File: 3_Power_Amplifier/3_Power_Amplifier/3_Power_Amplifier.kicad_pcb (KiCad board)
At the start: 2 copper layers, 100 x 100 mm, 15 parts, among them P1 IN_FUENTE_CONM, P2 OUT_CON_CAP, P3 OUT_SIN_CAP, P4 CONN_01X02, Q1 IRF740N, Q2 IRF740N, Q3 IRF740N, Q4 IRF740N, T1 TRANSFO-SO12

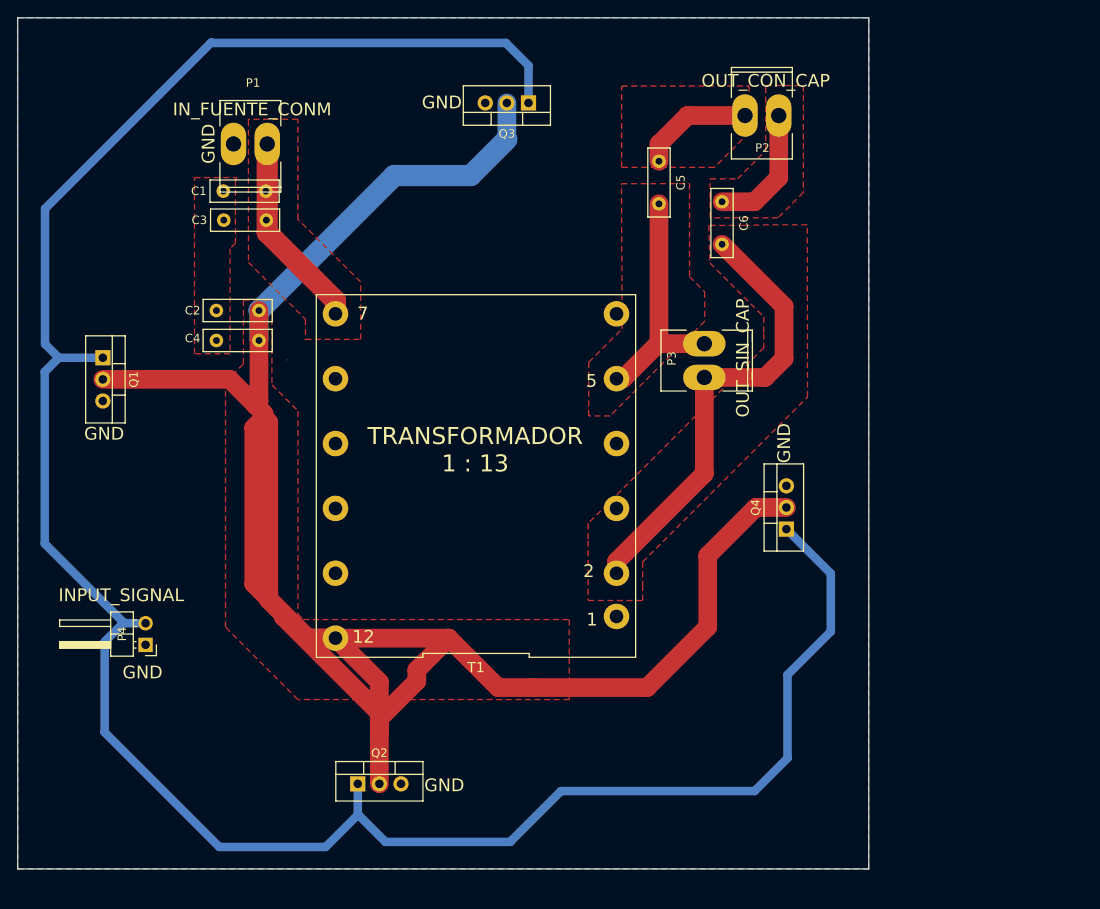
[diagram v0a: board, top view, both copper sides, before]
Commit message: AMPLIFICADOR DE POTENCIA_2 PCBS
el transformador con array capacitivo y mosfet con disipadores
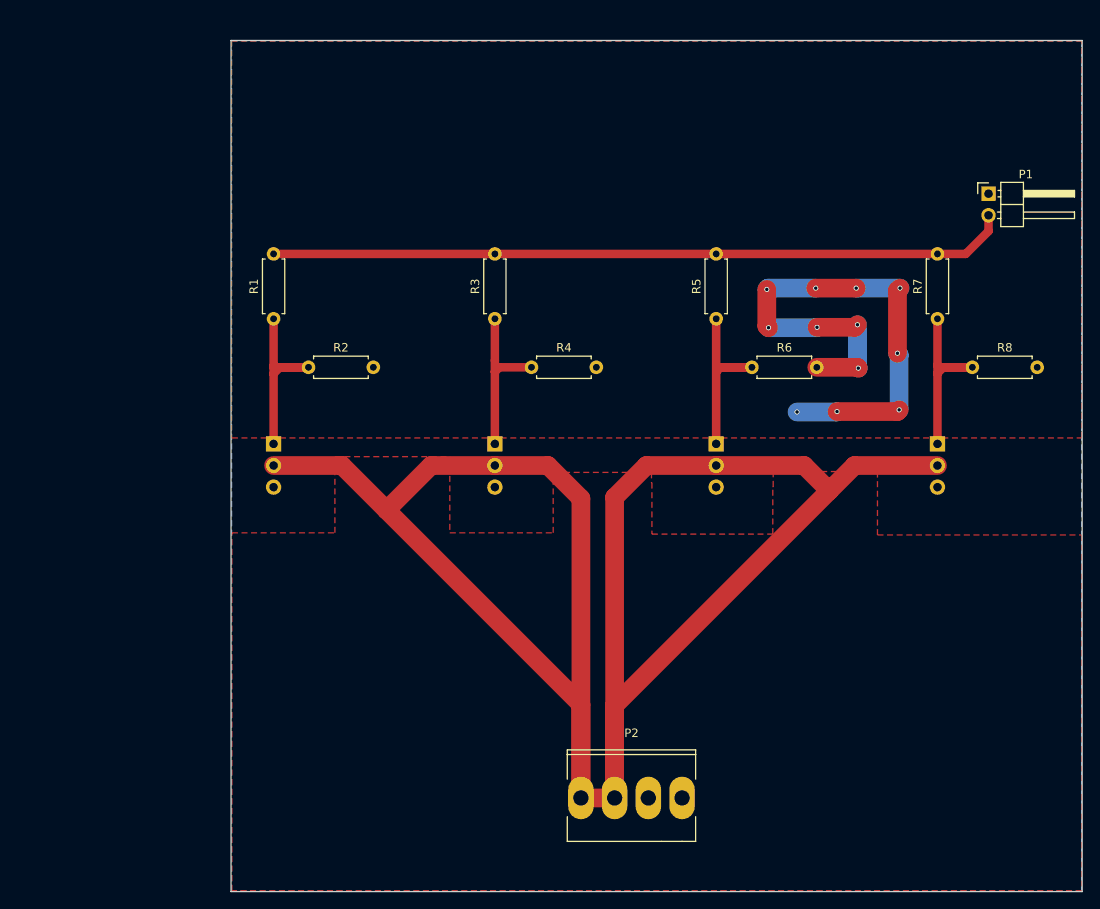
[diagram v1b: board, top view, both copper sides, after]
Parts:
- removed C1, C2, C3, C4, C5, C6: 32nF, Capacitors_THT:C_Disc_D8.0mm_W2.5mm_P5.00mm
- removed P3: OUT_SIN_CAP, Sockets_MOLEX_KK-System:Socket_MOLEX-KK-RM3-96mm_Lock_2pin_straight
- removed P4: CONN_01X02, Pin_Headers:Pin_Header_Angled_1x02_Pitch2.54mm
- removed T1: TRANSFO-SO12, libreria_Power_Amplifier_huellas:foot_print_trafo
- added R1: 100, Resistors_THT:R_Axial_DIN0207_L6.3mm_D2.5mm_P7.62mm_Horizontal, F.Cu at (83.5, 78.2)
- added R2: 10K, Resistors_THT:R_Axial_DIN0207_L6.3mm_D2.5mm_P7.62mm_Horizontal, F.Cu at (87.6, 83.9)
- added R3: 100, Resistors_THT:R_Axial_DIN0207_L6.3mm_D2.5mm_P7.62mm_Horizontal, F.Cu at (109.5, 78.2)
- added R4: 10K, Resistors_THT:R_Axial_DIN0207_L6.3mm_D2.5mm_P7.62mm_Horizontal, F.Cu at (113.8, 83.9)
- added R5: 100, Resistors_THT:R_Axial_DIN0207_L6.3mm_D2.5mm_P7.62mm_Horizontal, F.Cu at (135.5, 78.2)
- added R6: 10K, Resistors_THT:R_Axial_DIN0207_L6.3mm_D2.5mm_P7.62mm_Horizontal, F.Cu at (139.7, 83.9)
- added R7: 100, Resistors_THT:R_Axial_DIN0207_L6.3mm_D2.5mm_P7.62mm_Horizontal, F.Cu at (161.5, 78.2)
- added R8: 10K, Resistors_THT:R_Axial_DIN0207_L6.3mm_D2.5mm_P7.62mm_Horizontal, F.Cu at (165.6, 83.9)
- P1: value IN_FUENTE_CONM -> INPUT_SIGNAL; footprint Sockets_MOLEX_KK-System:Socket_MOLEX-KK-RM3-96mm_Lock_2pin_straight -> Pin_Headers:Pin_Header_Angled_1x02_Pitch2.54mm
- P2: value OUT_CON_CAP -> OUT_SWITCHEO; footprint Sockets_MOLEX_KK-System:Socket_MOLEX-KK-RM3-96mm_Lock_2pin_straight -> Sockets_MOLEX_KK-System:Socket_MOLEX-KK-RM3-96mm_Lock_4pin_straight
- Q1, Q2, Q3, Q4: footprint TO_SOT_Packages_THT:TO-220_Vertical -> libreria_Power_Amplifier_huellas:TO-220_Vertical
- moved P1 86.9 mm to (167.5, 63.5), turned to 0 degrees
- moved P2 81.6 mm to (125.5, 134.5)
- moved Q3 45.7 mm to (135.5, 92.9), turned to 270 degrees
- moved Q2 43.1 mm to (109.5, 92.9), turned to 270 degrees
- moved Q1 22.5 mm to (83.5, 92.9)
- moved Q4 20.4 mm to (161.5, 92.9), turned to 270 degrees
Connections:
- P1 pad 1: /ARRAY_CAP -> /GND
- P1 pad 2: /GND -> /DDS
- P2 pad 1: /OUT_SISTEM_ONE -> /SWITCHEO
- P2 pad 2: /OUT_SISTEM_TWO -> /SWITCHEO
- Q1 pad 1: /INPUT_SIGNAL -> Net-(Q1-Pad1)
- Q1 pad 2: /SIGNAL_PWM -> /SWITCHEO
- Q2 pad 1: /INPUT_SIGNAL -> Net-(Q2-Pad1)
- Q2 pad 2: /SIGNAL_PWM -> /SWITCHEO
- Q3 pad 1: /INPUT_SIGNAL -> Net-(Q3-Pad1)
- Q3 pad 2: /SIGNAL_PWM -> /SWITCHEO
- Q4 pad 1: /INPUT_SIGNAL -> Net-(Q4-Pad1)
- Q4 pad 2: /SIGNAL_PWM -> /SWITCHEO
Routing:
- net /INPUT_SIGNAL: track 273.5 -> 0.00 mm
- net /SIGNAL_PWM: track 260.3 -> 0.00 mm
- net /SWITCHEO: track 0.00 -> 248.3 mm
- net /DDS: track 0.00 -> 87.0 mm
- net /GND: track 0.00 -> 67.6 mm, vias 0 -> 12
- net /OUT_POT_TWO: track 54.0 -> 0.00 mm
- net /ARRAY_CAP: track 37.7 -> 0.00 mm
- net /OUT_POT_ONE: track 28.5 -> 0.00 mm
- net Net-(Q1-Pad1): track 0.00 -> 23.5 mm
- net Net-(Q3-Pad1): track 0.00 -> 23.3 mm
- net Net-(Q4-Pad1): track 0.00 -> 23.3 mm
- net Net-(Q2-Pad1): track 0.00 -> 19.2 mm
- net /OUT_SISTEM_TWO: track 15.1 -> 0.00 mm
- net /OUT_SISTEM_ONE: track 13.5 -> 0.00 mm
- added copper zone on F.Cu, net /GND
- added copper zone on F.Cu, net /SWITCHEO
- removed copper zone on F.Cu, net /ARRAY_CAP
- removed copper zone on F.Cu, net /OUT_POT_ONE
- removed copper zone on F.Cu, net /OUT_POT_TWO
- removed copper zone on F.Cu, net /OUT_SISTEM_ONE
- removed copper zone on F.Cu, net /OUT_SISTEM_TWO
- removed copper zone on F.Cu, net /SIGNAL_PWM
- removed copper zone on F.Cu, net Net-(C1-Pad2)
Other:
- board text removed: "1"
- board text removed: "12"
- board text removed: "2"
- board text removed: "5"
- board text removed: "7"
- board text removed: "GND"
- board text removed: "INPUT_SIGNAL"
- board text removed: "IN_FUENTE_CONM"
- board text removed: "OUT_CON_CAP"
- board text removed: "OUT_SIN_CAP"
- board text removed: "TRANSFORMADOR 1 : 13"

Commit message: AMPLIFICADOR DE POTENCIA_2 PCB_UNO
CON ISLETAS Y DISIPADORES VERTICALES
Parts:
- added P3: ISLETA, Mounting_Holes:MountingHole_3.2mm_M3_Pad_Via, F.Cu at (84.5, 139.5)
- added P4: ISLETA, Mounting_Holes:MountingHole_3.2mm_M3_Pad_Via, F.Cu at (172.5, 139.5)
- added P5: ISLETA, Mounting_Holes:MountingHole_3.2mm_M3_Pad_Via, F.Cu at (172.5, 51.5)
- added P6: ISLETA, Mounting_Holes:MountingHole_3.2mm_M3_Pad_Via, F.Cu at (84.5, 51.5)
- added P7: OUT_SWITCHEO, libreria_Power_Amplifier_huellas:Socket_MOLEX-2-pin-invertido, F.Cu at (124.6, 51.4)
- added P8: TIERRAA, Pin_Headers:Pin_Header_Straight_1x02_Pitch2.54mm, F.Cu at (83.0, 101.0)
- P1: footprint Pin_Headers:Pin_Header_Angled_1x02_Pitch2.54mm -> libreria_Power_Amplifier_huellas:Pin_Header_Pitch2.54mm_NEW
- P2: value OUT_SWITCHEO -> TIERRA; footprint Sockets_MOLEX_KK-System:Socket_MOLEX-KK-RM3-96mm_Lock_4pin_straight -> libreria_Power_Amplifier_huellas:Socket_MOLEX-2-pin-invertido
- Q1, Q2, Q3, Q4: value IRF740N -> IRF740NPBF; footprint libreria_Power_Amplifier_huellas:TO-220_Vertical -> libreria_Power_Amplifier_huellas:TO-220_Ver_Disipador
- R1, R2, R3, R4, R5, R6, R7, R8: footprint Resistors_THT:R_Axial_DIN0207_L6.3mm_D2.5mm_P7.62mm_Horizontal -> libreria_Power_Amplifier_huellas:R_Axia_P7.62mm_Horizontal_INV
- moved P1 84.7 mm to (128.4, 138.6), turned to 270 degrees
- moved P2 83.4 mm to (132.2, 51.4)
- moved R1 33.3 mm to (103.2, 105.1), turned to 270 degrees
- moved R3 30.5 mm to (123.6, 105.2), turned to 270 degrees
- moved R2 29.4 mm to (108.0, 105.1), turned to 270 degrees
- moved R5 28.4 mm to (144.9, 105.0), turned to 270 degrees
- moved R7 27.6 mm to (165.5, 105.5), turned to 270 degrees
- moved R4 25.9 mm to (128.5, 105.2), turned to 270 degrees
- moved R6 23.1 mm to (149.1, 105.0), turned to 270 degrees
- moved R8 22.0 mm to (170.0, 105.5), turned to 270 degrees
- moved Q1 18.7 mm to (102.0, 95.5)
- moved Q2 12.8 mm to (122.0, 95.5)
- moved Q3 7.94 mm to (143.0, 95.5)
- moved Q4 3.00 mm to (163.0, 95.5)
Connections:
- P1 pad 1: /GND -> /DDS
- P1 pad 2: /DDS -> /GND
- P2 pad 1: /SWITCHEO -> /GND
- P2 pad 2: /SWITCHEO -> /GND
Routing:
- net /SWITCHEO: track 248.3 -> 0.00 mm
- net /DDS: track 87.0 -> 0.00 mm
- net /GND: track 67.6 -> 28.2 mm, vias 12 -> 6
- net Net-(Q1-Pad1): track 23.5 -> 12.4 mm
- net Net-(Q3-Pad1): track 23.3 -> 12.3 mm
- net Net-(Q4-Pad1): track 23.3 -> 13.6 mm
- net Net-(Q2-Pad1): track 19.2 -> 13.2 mm
- added copper zone on F.Cu, net /DDS
- added copper zone on F.Cu, net Net-(Q1-Pad1)
- added copper zone on F.Cu, net Net-(Q2-Pad1)
- added copper zone on F.Cu, net Net-(Q3-Pad1)
- added copper zone on F.Cu, net Net-(Q4-Pad1)
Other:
- board text added: "3_POWER AMPLIFIER PART_1"
- board text added: "DDS"
- board text added: "GND"
- board text added: "SWITCHEO"

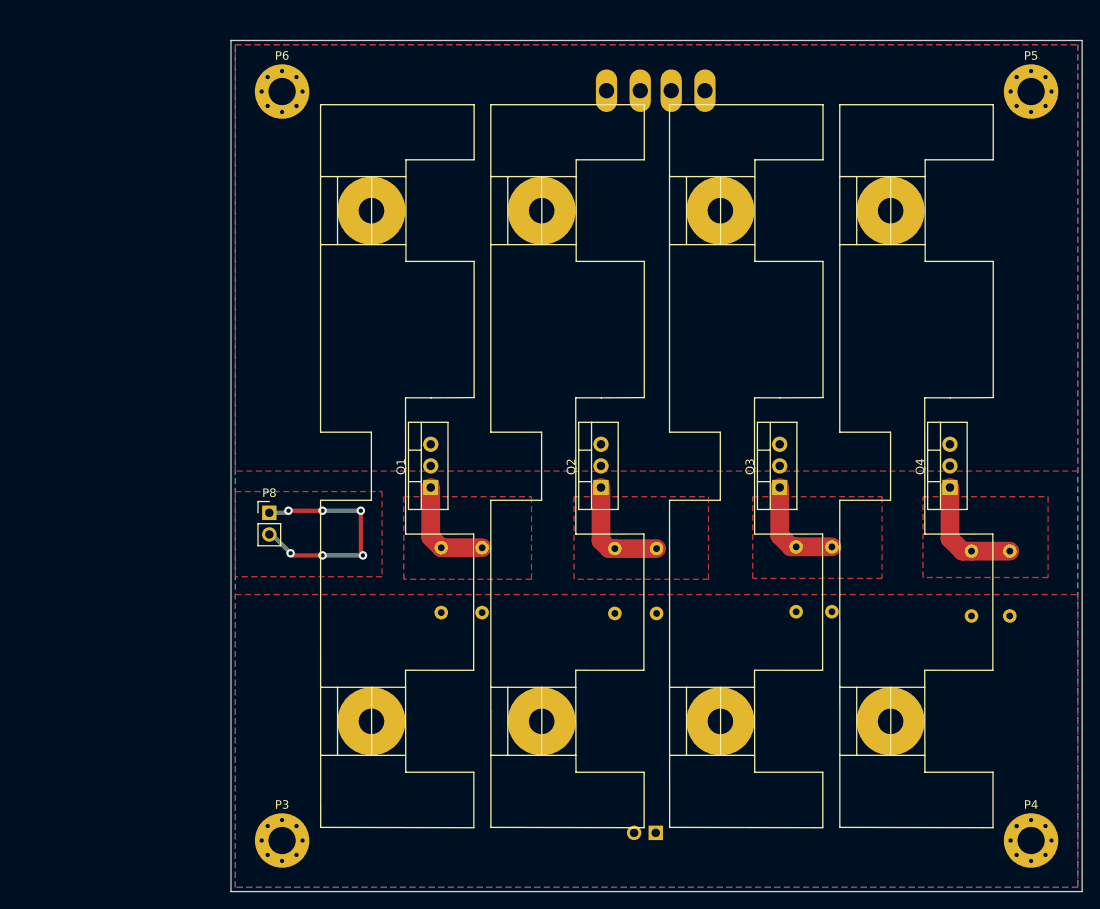
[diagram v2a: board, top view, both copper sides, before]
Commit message: AMPLIFICADOR DE POTENCIA_2 PCB_V3
MODIFICACION DE HUELLAS DEL COOLER Y PLANOS A SOLIDOS
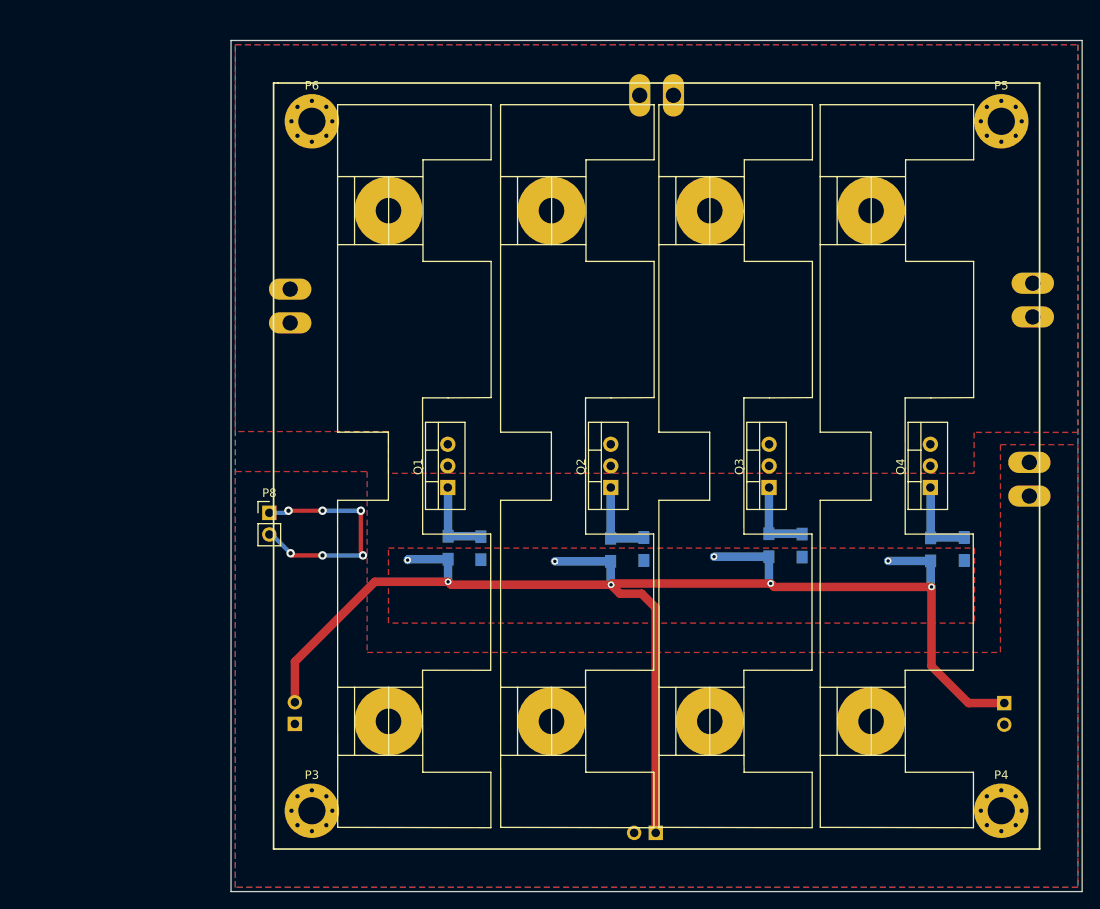
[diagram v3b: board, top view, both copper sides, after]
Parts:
- added P10: SWITCHED_POWER_INV, libreria_Power_Amplifier_huellas:INV_Socket_MOLEX-2-pines, F.Cu at (172.7, 76.0)
- added P11: SIGNAL_INPUT, libreria_Power_Amplifier_huellas:REDISEÑADO_INV_Pin_Header_Pitch2.54mm, F.Cu at (86.0, 125.8)
- added P12: SWITCHED_POWER_INV, libreria_Power_Amplifier_huellas:INV_Socket_MOLEX-2-pines, F.Cu at (85.5, 76.7)
- added P9: TIERRA, libreria_Power_Amplifier_huellas:INV_Socket_MOLEX-2-pines, F.Cu at (172.3, 97.0)
- P1: value INPUT_SIGNAL -> SIGNAL_INPUT; footprint libreria_Power_Amplifier_huellas:Pin_Header_Pitch2.54mm_NEW -> libreria_Power_Amplifier_huellas:REDISEÑADO_INV_Pin_Header_Pitch2.54mm
- P2: value TIERRA -> SWITCHED_POWER_INV; footprint libreria_Power_Amplifier_huellas:Socket_MOLEX-2-pin-invertido -> libreria_Power_Amplifier_huellas:INV_Socket_MOLEX-2-pines
- P7: value OUT_SWITCHEO -> SIGNAL_INPUT; footprint libreria_Power_Amplifier_huellas:Socket_MOLEX-2-pin-invertido -> libreria_Power_Amplifier_huellas:REDISEÑADO_INV_Pin_Header_Pitch2.54mm
- R1, R2, R3, R4, R5, R6, R7, R8: footprint libreria_Power_Amplifier_huellas:R_Axia_P7.62mm_Horizontal_INV -> libreria_Power_Amplifier_huellas:INV_R_0805_HandSoldering
- moved P7 84.7 mm to (169.3, 123.3)
- moved R8 5.36 mm to (164.7, 105.2)
- moved P3 4.95 mm to (88.0, 136.0)
- moved P4 4.95 mm to (169.0, 136.0)
- moved P5 4.95 mm to (169.0, 55.0)
- moved P6 4.95 mm to (88.0, 55.0)
- moved R7 4.80 mm to (160.7, 105.3)
- moved P2 3.74 mm to (128.5, 52.0)
- moved R6 3.50 mm to (145.6, 104.8)
- moved R5 3.21 mm to (141.7, 104.8)
- moved Q4 2.30 mm to (160.7, 95.5)
- moved Q1 2.00 mm to (104.0, 95.5)
- moved R4 1.50 mm to (127.0, 105.2)
- moved Q3 1.25 mm to (141.8, 95.5)
- moved Q2 1.15 mm to (123.2, 95.5)
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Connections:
- P2 pad 1: /GND -> /SWITCHED_POWER
- P2 pad 2: /GND -> /SWITCHED_POWER
- P7 pad 1: /SWITCHEO -> /DDS
- P7 pad 2: /SWITCHEO -> /GND
- Q1 pad 2: /SWITCHEO -> /SWITCHED_POWER
- Q2 pad 2: /SWITCHEO -> /SWITCHED_POWER
- Q3 pad 2: /SWITCHEO -> /SWITCHED_POWER
- Q4 pad 2: /SWITCHEO -> /SWITCHED_POWER
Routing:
- net /DDS: track 0.00 -> 170.8 mm, vias 0 -> 8
- net Net-(Q4-Pad1): track 13.6 -> 9.91 mm
- net Net-(Q2-Pad1): track 13.2 -> 9.92 mm
- net Net-(Q3-Pad1): track 12.3 -> 9.35 mm
- net Net-(Q1-Pad1): track 12.4 -> 9.61 mm
- added copper zone on F.Cu, net /SWITCHED_POWER
- removed copper zone on F.Cu, net /SWITCHEO
- removed copper zone on F.Cu, net Net-(Q1-Pad1)
- removed copper zone on F.Cu, net Net-(Q2-Pad1)
- removed copper zone on F.Cu, net Net-(Q3-Pad1)
- removed copper zone on F.Cu, net Net-(Q4-Pad1)
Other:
- board text added: "SWITCHED_POWER"
- board text removed: "SWITCHEO"

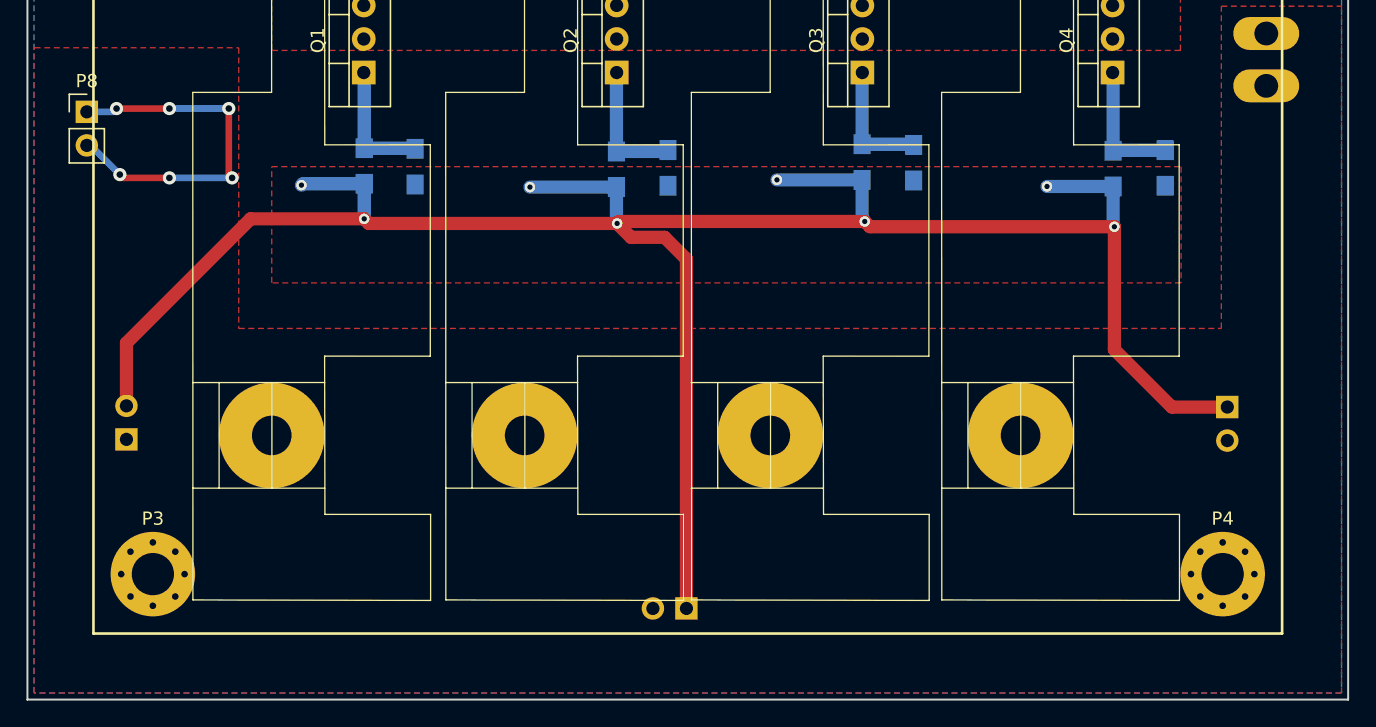
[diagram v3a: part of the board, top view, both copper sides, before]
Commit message: AMPLIFICADOR DE POTENCIA_2 PCB_V4
VIAS PARA PLANO DE TIERRA
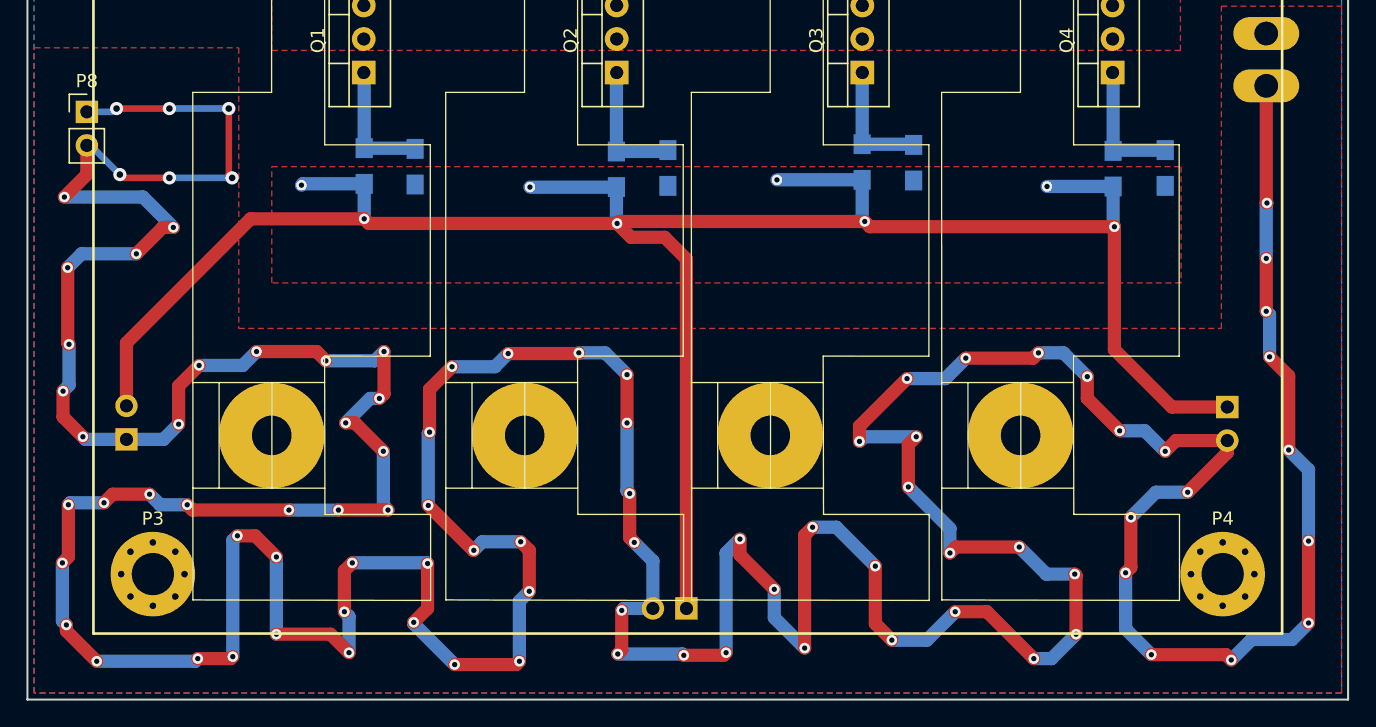
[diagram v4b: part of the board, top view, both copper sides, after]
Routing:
- net /GND: track 28.2 -> 485.8 mm, vias 6 -> 92
